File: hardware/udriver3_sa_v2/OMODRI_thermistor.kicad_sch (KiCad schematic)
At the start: 9 parts, among them U16 OPA333xxDCK

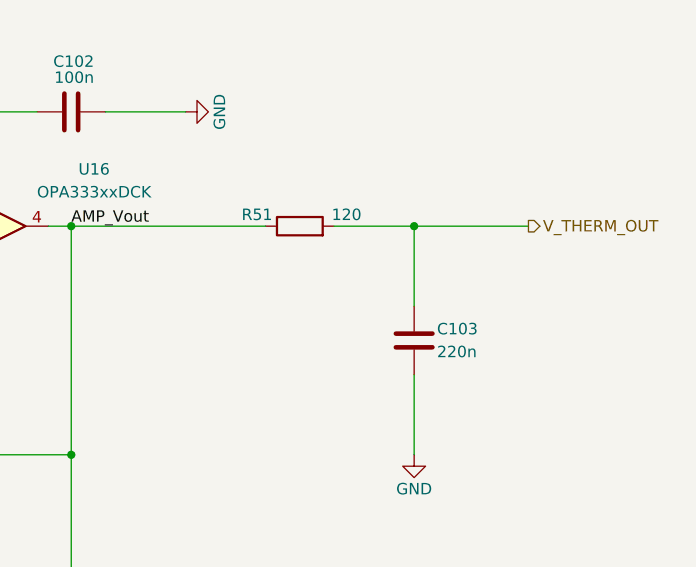
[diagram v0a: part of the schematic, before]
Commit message: Partial update of uOmodri Single Axis V2.
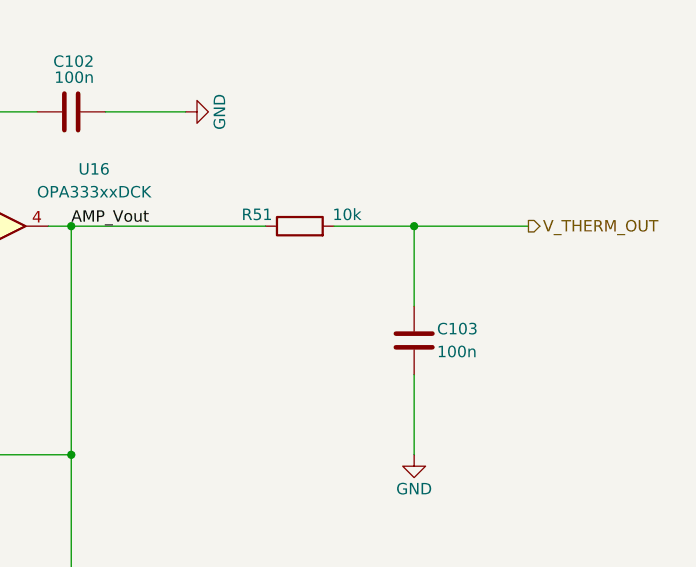
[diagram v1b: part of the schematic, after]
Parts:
- C103: value 220n -> 100n; DigiKey 490-17040-1-ND -> 490-12686-1-ND; Farnell 3582770 -> 2990693; LCSC C161474 -> C76939; Mouser 81-GRM033R61C224KE4D -> 81-GRM033R61E104KE4D; Part No GRM033R61C224KE14D -> GRM033R61E104KE14D; RS (none) -> 185-2066
- R51: value 120 -> 10k; DigiKey P122692CT-ND -> P122414CT-ND; Farnell 2396857 -> 2302362; LCSC C278569 -> C717002; Mouser 667-ERJ-1GNF1200C -> 667-ERJ-1GNF1002C; Part No ERJ1GNF1200C -> ERJ1GNF1002C; RS (none) -> 176-3597
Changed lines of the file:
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@@
 			)
 		)
-		(property "Value" "120"
+		(property "Value" "10k"
 			(at 171.958 100.33 90)
 			(effects
@@
 			)
 		)
-		(property "Datasheet" "https://industrial.panasonic.com/sa/products/pt/general-purpose-chip-resistors/models/ERJ1GNF1200C"
-			(at 165.1 101.6 0)
-			(effects
-				(font
-					(size 1.27 1.27)
-				)
-				(hide yes)
-			)
-		)
-		(property "Description" "0201,120Ω, 0.05W, ±1%, SMD  resistor"
-			(at 165.1 101.6 0)
-			(effects
-				(font
-					(size 1.27 1.27)
-				)
-				(hide yes)
-			)
-		)
-		(property "DigiKey" "P122692CT-ND"
-			(at 165.1 101.6 0)
-			(effects
-				(font
-					(size 1.27 1.27)
-				)
-				(hide yes)
-			)
-		)
-		(property "Farnell" "2396857"
-			(at 165.1 101.6 0)
-			(effects
-				(font
-					(size 1.27 1.27)
-				)
-				(hide yes)
-			)
-		)
-		(property "Mouser" "667-ERJ-1GNF1200C"
-			(at 165.1 101.6 0)
-			(effects
-				(font
-					(size 1.27 1.27)
-				)
-				(hide yes)
-			)
-		)
-		(property "Part No" "ERJ1GNF1200C"
-			(at 165.1 101.6 0)
-			(effects
-				(font
-					(size 1.27 1.27)
-				)
-				(hide yes)
-			)
-		)
-		(property "RS" ""
-			(at 165.1 101.6 0)
-			(effects
-				(font
-					(size 1.27 1.27)
-				)
-				(hide yes)
-			)
-		)
-		(property "LCSC" "C278569"
+		(property "Datasheet" "https://industrial.panasonic.com/sa/products/pt/general-purpose-chip-resistors/models/ERJ1GNF1002C"
+			(at 165.1 101.6 0)
+			(effects
+				(font
+					(size 1.27 1.27)
+				)
+				(hide yes)
+			)
+		)
+		(property "Description" "0201, 10kΩ, 0.05W, ±1%, SMD  resistor"
+			(at 165.1 101.6 0)
+			(effects
+				(font
+					(size 1.27 1.27)
+				)
+				(hide yes)
+			)
+		)
+		(property "DigiKey" "P122414CT-ND"
+			(at 165.1 101.6 0)
+			(effects
+				(font
+					(size 1.27 1.27)
+				)
+				(hide yes)
+			)
+		)
+		(property "Farnell" "2302362"
+			(at 165.1 101.6 0)
+			(effects
+				(font
+					(size 1.27 1.27)
+				)
+				(hide yes)
+			)
+		)
+		(property "Mouser" "667-ERJ-1GNF1002C"
+			(at 165.1 101.6 0)
+			(effects
+				(font
+					(size 1.27 1.27)
+				)
+				(hide yes)
+			)
+		)
+		(property "Part No" "ERJ1GNF1002C"
+			(at 165.1 101.6 0)
+			(effects
+				(font
+					(size 1.27 1.27)
+				)
+				(hide yes)
+			)
+		)
+		(property "RS" "176-3597"
+			(at 165.1 101.6 0)
+			(effects
+				(font
+					(size 1.27 1.27)
+				)
+				(hide yes)
+			)
+		)
+		(property "LCSC" "C717002"
 			(at 165.1 101.6 0)
 			(effects
@@
 			(project "omodri_sa_laas"
 				(path "/de5b13f0-933a-4c4d-9979-13dc57b13241/b535f441-e5f2-4a7b-a0a6-02c4bb8f1fa2"
+					(reference "R51")
+					(unit 1)
+				)
+				(path "/de5b13f0-933a-4c4d-9979-13dc57b13241/00000000-0000-0000-0000-00005f3a3f16/f2e4b637-b410-4c88-a5bd-ca173e5a2c6b"
 					(reference "R51")
 					(unit 1)
@@
 			)
 		)
-		(property "Value" "220n"
+		(property "Value" "100n"
 			(at 180.34 115.57 0)
 			(effects
@@
 			)
 		)
-		(property "Datasheet" "https://www.murata.com/en-eu/products/productdetail?partno=GRM033R61C224KE14%23"
+		(property "Datasheet" "https://www.murata.com/en-eu/products/productdetail?partno=GRM033R61E104KE14%23"
 			(at 177.8 114.3 0)
 			(effects
@@
 			)
 		)
-		(property "Description" "0201, 220nf, 16V,  ±10%, X5R, SMD MLCC"
+		(property "Description" "0201, 100nf, 25V,  ±10%, X5R, SMD MLCC"
 			(at 177.8 114.3 0)
 			(effects
@@
 			)
 		)
-		(property "DigiKey" "490-17040-1-ND"
+		(property "DigiKey" "490-12686-1-ND"
 			(at 177.8 114.3 0)
 			(effects
@@
 			)
 		)
-		(property "Farnell" "3582770"
+		(property "Farnell" "2990693"
 			(at 177.8 114.3 0)
 			(effects
@@
 			)
 		)
-		(property "Mouser" "81-GRM033R61C224KE4D"
+		(property "Mouser" "81-GRM033R61E104KE4D"
 			(at 177.8 114.3 0)
 			(effects
@@
 			)
 		)
-		(property "Part No" "GRM033R61C224KE14D"
+		(property "Part No" "GRM033R61E104KE14D"
 			(at 177.8 114.3 0)
 			(effects
@@
 			)
 		)
-		(property "RS" ""
+		(property "RS" "185-2066"
 			(at 177.8 114.3 0)
 			(effects
@@
 			)
 		)
-		(property "LCSC" "C161474"
+		(property "LCSC" "C76939"
 			(at 177.8 114.3 0)
 			(effects
